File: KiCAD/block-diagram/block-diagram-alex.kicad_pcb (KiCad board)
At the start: 4 copper layers, 50.8 x 38.1 mm, 34 parts, among them J1 Conn_01x08, J2 Conn_01x08, J3 Conn_01x10, Q3 NMOS, Q4 NMOS, U1 74LS02, U3 74LS11, U6 LMC555xM

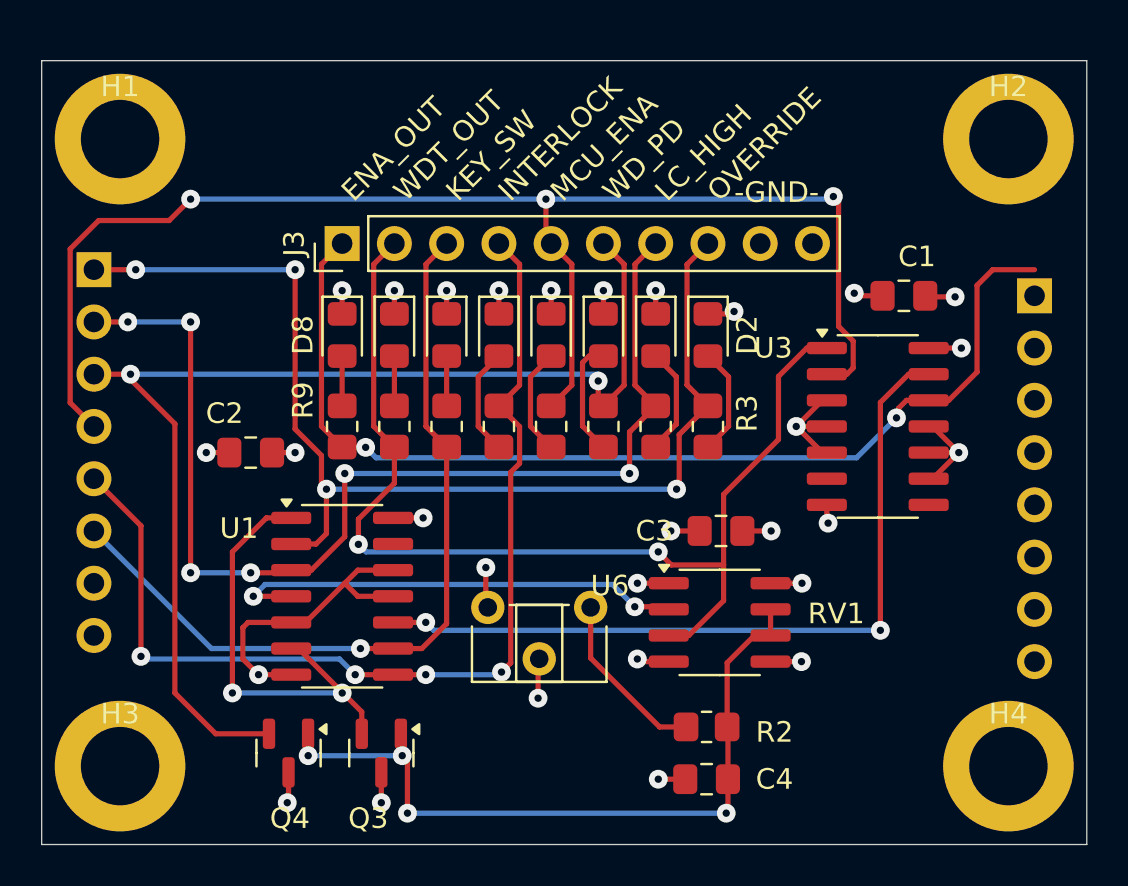
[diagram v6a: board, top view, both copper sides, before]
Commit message: Finishing Touches before adding Part and Cfg Nums
*  Fix silkscreen text overlaps
*  Move J2 up or down .05" and fix routing
*  Disconnect 555 pin 5 from GND and add a 10uF capacitor
*  Change U1, U3 from 74LS--- to 74HC---
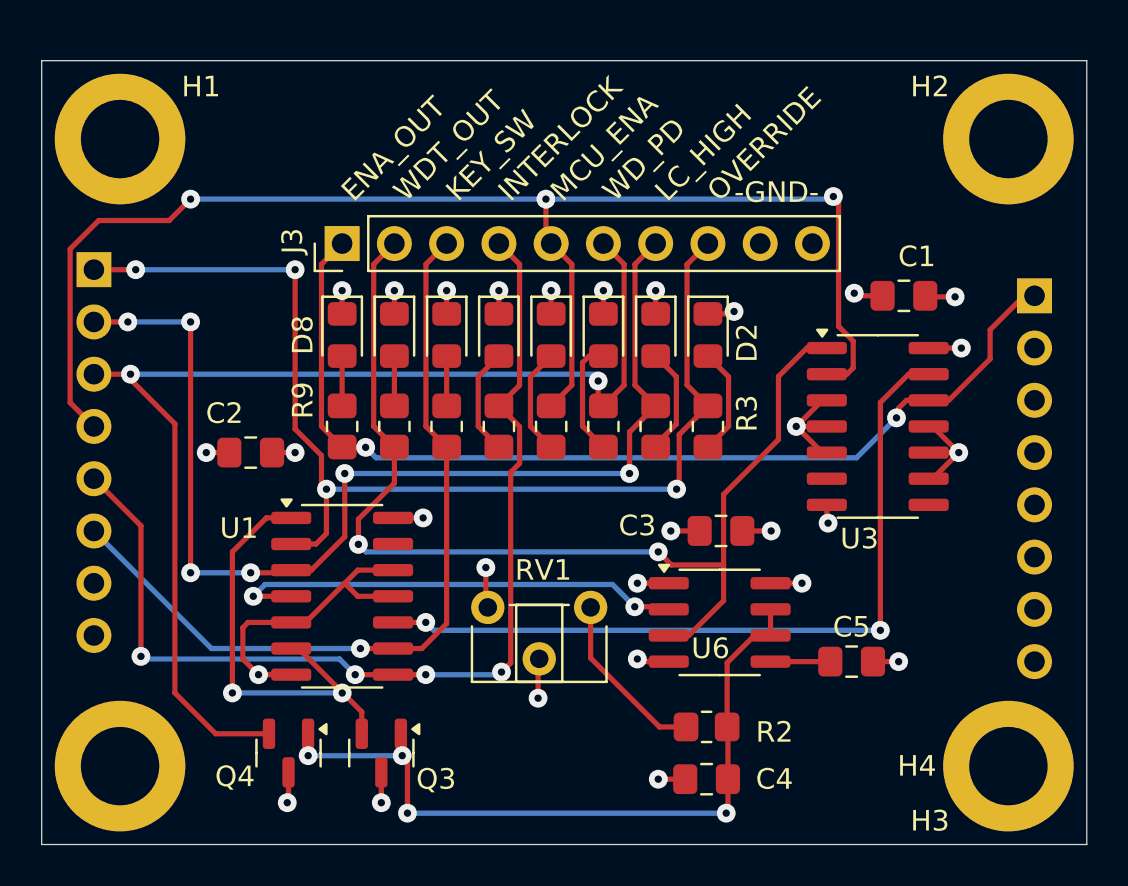
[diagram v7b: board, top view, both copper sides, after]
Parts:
- added C5: C_Small, Capacitor_SMD:C_0805_2012Metric_Pad1.18x1.45mm_HandSolder, F.Cu at (158.8, 100.3)
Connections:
- U6 pad 5: GND -> Net-(U6-CV)
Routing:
- net Net-(U6-CV): track 0.00 -> 2.90 mm
- net /LASER_ENA: track 51.2 -> 49.0 mm

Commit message: Rev 1.0 as built
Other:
- board text added: "SCOS Safety Circuit V1.0 - 2024-05 A. Howard, E. Hazen"
- board text added: "V1.0 5/24"
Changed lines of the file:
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@@
 		(allow_soldermask_bridges_in_footprints no)
 		(pcbplotparams
-			(layerselection 0x00010fc_ffffffff)
+			(layerselection 0x00010f0_ffffffff)
 			(plot_on_all_layers_selection 0x0000000_00000000)
 			(disableapertmacros no)
@@
 			(outputformat 1)
 			(mirror no)
-			(drillshape 1)
+			(drillshape 0)
 			(scaleselection 1)
-			(outputdirectory "")
+			(outputdirectory "gerber/")
 		)
 	)
@@
 		(layer "Edge.Cuts")
 	)
+	(gr_text "SCOS Safety Circuit\nV1.0 - 2024-05\nA. Howard, E. Hazen"
+		(at 157.226 78.74 0)
+		(layer "B.SilkS")
+		(effects
+			(font
+				(size 1.651 1.651)
+				(thickness 0.2032)
+			)
+			(justify left bottom mirror)
+		)
+	)
 	(gr_text "-GND-"
 		(at 153.035 78.105 0)
 		(layer "F.SilkS")
 		(effects
+			(font
+				(size 1 1)
+				(thickness 0.1)
+			)
+			(justify left bottom)
+		)
+	)
+	(gr_text "V1.0 5/24"
+		(at 140.462 108.458 0)
+		(layer "F.SilkS")
+		(effects
